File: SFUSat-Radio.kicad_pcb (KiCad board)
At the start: 4 copper layers, 95.9 x 90.2 mm, 279 parts, among them J1 PC104-8BIT, J10 TP_TH_150, J11 TP_TH_150, J12 SMA, J13 SMA, J14 SMA, J15 Conn_01x02, J16 SMA, J17 SMA, J18 SMA, J19 Conn_01x03, J2 PC104PTH, J20 Conn_01x03, J21 TP_TH_150, J22 TP_TH_150, J23 TP_TH_150, J24 TP_TH_150, J25 Conn_01x02, J3 PC104PTH, J4 PC104PTH, J400 SMA, J401 TP_TH_150, J402 TP_TH_150, J404 TP_TH_150, J405 TP_TH_150, J406 TP_TH_150, J5 PC104PTH, J500 SMA, J501 TP_TH_150, J502 TP_TH_150, J504 TP_TH_150, J505 TP_TH_150, J506 TP_TH_150, J6 SMA, J7 TP_TH_150, J8 TP_TH_150, J9 TP_TH_150, U1 SINGLE_0402, U10 TPS799, U100 CC1101-Q1, U101 0433BM15A0001, U11 SINGLE_0402, U110 CC1101-Q1, U111 0915BM15A0001E, U12 CONN_02X05_SHRD, U13 CONN_02X05_SHRD, U14 2N7002DW, U15 TPS62175DQCR, U16 TPS71750DSER, U17 74LVC1G14SE-7, U2 SKY13345-368LF, U3 CD4555BPWR, U4 LMS3635AQRNLRQ1, U400 SINGLE_0402, U401 LMV358, U402 RF6886, U420 2N7002DW, U5 MML09211H, U500 SINGLE_0402, U501 LMV358, U502 RF6886, U6 SINGLE_0402, U600 STLM75, U610 STLM75, U7 SKY13372-467LF, U8 SINGLE_0402, U9 TLV702, X100 NX3225GA, X110 NX3225GA

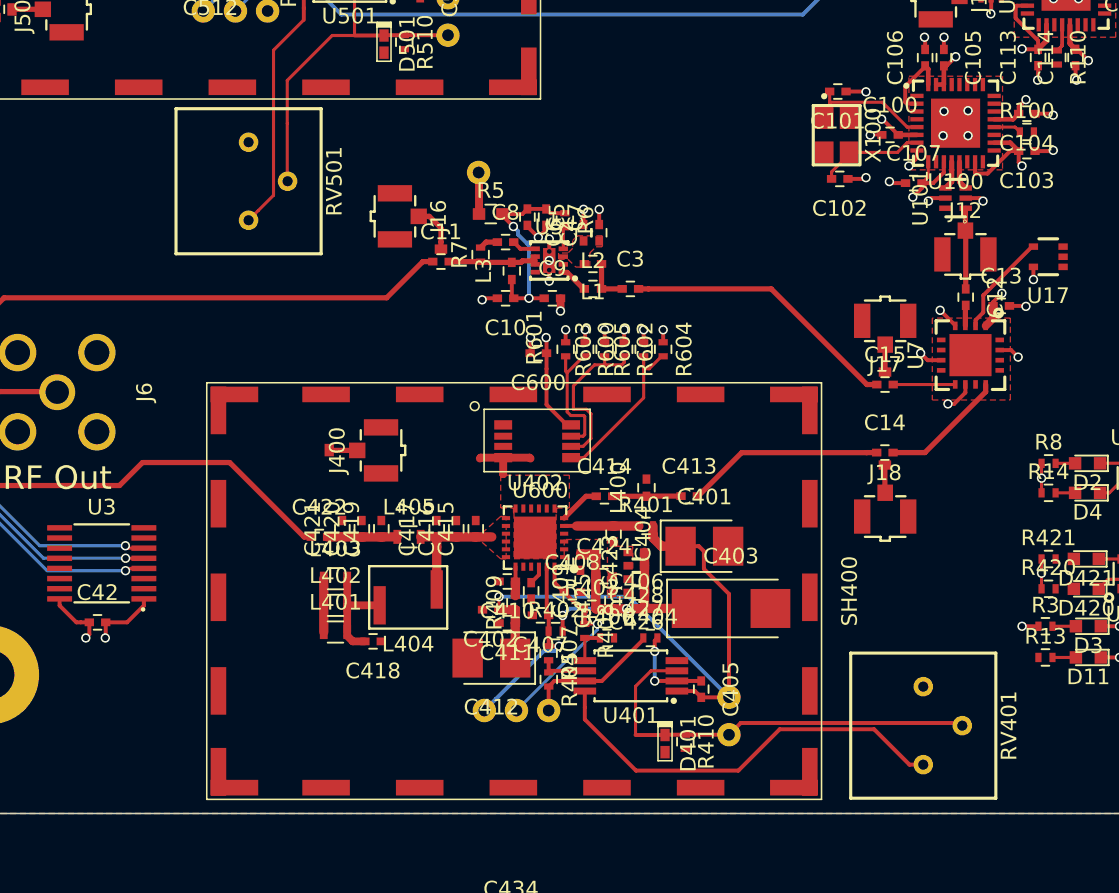
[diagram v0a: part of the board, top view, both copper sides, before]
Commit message: added optional gain select resistor
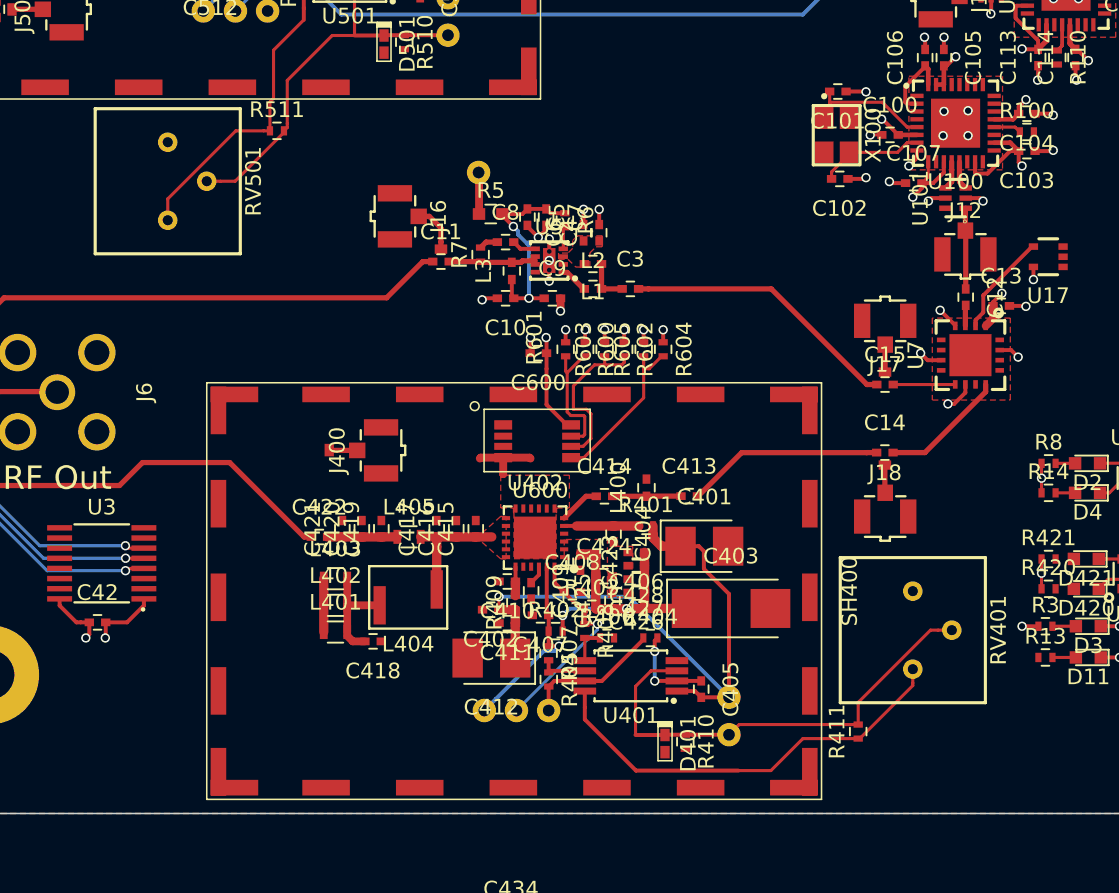
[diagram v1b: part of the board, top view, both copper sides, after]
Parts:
- added R411: DNP, SFUSat:R_0402, F.Cu at (173.2, 143.2)
- added R511: DNP, SFUSat:R_0402, F.Cu at (136.0, 104.8)
- moved RV401 6.16 mm to (176.8, 136.8)
- moved RV501 5.18 mm to (129.0, 108.0)
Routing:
- net /3V1: track 111.6 -> 115.7 mm
- net /PA_UB/GAIN: track 24.2 -> 27.4 mm
- net /PA_LB/GAIN: track 27.5 -> 30.1 mm
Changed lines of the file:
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@@
 (kicad_pcb (version 4) (host pcbnew 4.0.7-e2-6376~58~ubuntu16.04.1)
   (general
-    (links 720)
-    (no_connects 107)
-    (area 45.1 55.986 358.142847 234.47)
+    (links 724)
+    (no_connects 99)
+    (area 112.449999 58.279999 208.440001 148.550001)
     (thickness 1.6)
     (drawings 18)
-    (tracks 1119)
+    (tracks 1132)
     (zones 0)
-    (modules 279)
+    (modules 281)
     (nets 207)
   )
@@
   )
   (setup
-    (last_trace_width 0.254)
+    (last_trace_width 0.2)
     (user_trace_width 0.1524)
     (user_trace_width 0.2)
@@
   )
   (module SFUSat:CT6EP103 locked (layer F.Cu)
-    (at 177.42 142.87 270)
+    (at 176.75 136.75 270)
     (fp_text reference RV401 (at 0 -5.5 270) (layer F.SilkS)
       (effects (font (size 1 1) (thickness 0.15)))
@@
   )
   (module SFUSat:CT6EP103 locked (layer F.Cu)
-    (at 134.18 107.98 270)
+    (at 129 107.98 270)
     (fp_text reference RV501 (at 0 -5.5 270) (layer F.SilkS)
       (effects (font (size 1 1) (thickness 0.15)))
@@
     )
   )
+  (module SFUSat:R_0402 (layer F.Cu)
+    (at 173.25 143.25 90)
+    (descr "Resistor SMD 0402, reflow soldering, Vishay (see dcrcw.pdf)")
+    (tags "resistor 0402")
+    (attr smd)
+    (fp_text reference R411 (at 0 -1.35 90) (layer F.SilkS)
+      (effects (font (size 1 1) (thickness 0.15)))
+    )
+    (fp_text value DNP (at 0 1.45 90) (layer F.Fab)
+      (effects (font (size 1 1) (thickness 0.15)))
+    )
+    (fp_text user %R (at 0 -1.35 90) (layer F.Fab)
+      (effects (font (size 1 1) (thickness 0.15)))
+    )
+    (fp_line (start -0.5 0.25) (end -0.5 -0.25) (layer F.Fab) (width 0.1))
+    (fp_line (start 0.5 0.25) (end -0.5 0.25) (layer F.Fab) (width 0.1))
+    (fp_line (start 0.5 -0.25) (end 0.5 0.25) (layer F.Fab) (width 0.1))
+    (fp_line (start -0.5 -0.25) (end 0.5 -0.25) (layer F.Fab) (width 0.1))
+    (fp_line (start 0.25 -0.53) (end -0.25 -0.53) (layer F.SilkS) (width 0.12))
+    (fp_line (start -0.25 0.53) (end 0.25 0.53) (layer F.SilkS) (width 0.12))
+    (fp_line (start -0.8 -0.45) (end 0.8 -0.45) (layer F.CrtYd) (width 0.05))
+    (fp_line (start -0.8 -0.45) (end -0.8 0.45) (layer F.CrtYd) (width 0.05))
+    (fp_line (start 0.8 0.45) (end 0.8 -0.45) (layer F.CrtYd) (width 0.05))
+    (fp_line (start 0.8 0.45) (end -0.8 0.45) (layer F.CrtYd) (width 0.05))
+    (pad 1 smd rect (at -0.45 0 90) (size 0.4 0.6) (layers F.Cu F.Paste F.Mask)
+      (net 116 /3V1) (solder_paste_margin -0.02))
+    (pad 2 smd rect (at 0.45 0 90) (size 0.4 0.6) (layers F.Cu F.Paste F.Mask)
+      (net 103 /PA_LB/GAIN) (solder_paste_margin -0.02))
+    (model Resistors_SMD.3dshapes/R_0402.wrl
+      (at (xyz 0 0 0))
+      (scale (xyz 1 1 1))
+      (rotate (xyz 0 0 0))
+    )
+  )
+  (module SFUSat:R_0402 (layer F.Cu)
+    (at 136 104.75)
+    (descr "Resistor SMD 0402, reflow soldering, Vishay (see dcrcw.pdf)")
+    (tags "resistor 0402")
+    (attr smd)
+    (fp_text reference R511 (at 0 -1.35) (layer F.SilkS)
+      (effects (font (size 1 1) (thickness 0.15)))
+    )
+    (fp_text value DNP (at 0 1.45) (layer F.Fab)
+      (effects (font (size 1 1) (thickness 0.15)))
+    )
+    (fp_text user %R (at 0 -1.35) (layer F.Fab)
+      (effects (font (size 1 1) (thickness 0.15)))
+    )
+    (fp_line (start -0.5 0.25) (end -0.5 -0.25) (layer F.Fab) (width 0.1))
+    (fp_line (start 0.5 0.25) (end -0.5 0.25) (layer F.Fab) (width 0.1))
+    (fp_line (start 0.5 -0.25) (end 0.5 0.25) (layer F.Fab) (width 0.1))
+    (fp_line (start -0.5 -0.25) (end 0.5 -0.25) (layer F.Fab) (width 0.1))
+    (fp_line (start 0.25 -0.53) (end -0.25 -0.53) (layer F.SilkS) (width 0.12))
+    (fp_line (start -0.25 0.53) (end 0.25 0.53) (layer F.SilkS) (width 0.12))
+    (fp_line (start -0.8 -0.45) (end 0.8 -0.45) (layer F.CrtYd) (width 0.05))
+    (fp_line (start -0.8 -0.45) (end -0.8 0.45) (layer F.CrtYd) (width 0.05))
+    (fp_line (start 0.8 0.45) (end 0.8 -0.45) (layer F.CrtYd) (width 0.05))
+    (fp_line (start 0.8 0.45) (end -0.8 0.45) (layer F.CrtYd) (width 0.05))
+    (pad 1 smd rect (at -0.45 0) (size 0.4 0.6) (layers F.Cu F.Paste F.Mask)
+      (net 116 /3V1) (solder_paste_margin -0.02))
+    (pad 2 smd rect (at 0.45 0) (size 0.4 0.6) (layers F.Cu F.Paste F.Mask)
+      (net 108 /PA_UB/GAIN) (solder_paste_margin -0.02))
+    (model Resistors_SMD.3dshapes/R_0402.wrl
+      (at (xyz 0 0 0))
+      (scale (xyz 1 1 1))
+      (rotate (xyz 0 0 0))
+    )
+  )
   (dimension 9.4 (width 0.3) (layer Dwgs.User)
     (gr_text "9.400 mm" (at 117.2 117.85) (layer Dwgs.User)
@@
   (segment (start 191.529999 127.349999) (end 191.63 127.45) (width 0.2) (layer F.Cu) (net 102))
   (segment (start 191.63 127.45) (end 191.63 127.95) (width 0.2) (layer F.Cu) (net 102))
-  (segment (start 164.97 143.45) (end 165.719999 142.700001) (width 0.254) (layer F.Cu) (net 103))
-  (segment (start 165.719999 142.700001) (end 179.750001 142.700001) (width 0.254) (layer F.Cu) (net 103))
-  (segment (start 179.750001 142.700001) (end 179.92 142.87) (width 0.2) (layer F.Cu) (net 103))
+  (segment (start 173.25 142.8) (end 173.25 141.380998) (width 0.2) (layer F.Cu) (net 103))
+  (segment (start 173.25 141.380998) (end 177.880998 136.75) (width 0.2) (layer F.Cu) (net 103))
+  (segment (start 178.366117 136.75) (end 179.25 136.75) (width 0.2) (layer F.Cu) (net 103))
+  (segment (start 177.880998 136.75) (end 178.366117 136.75) (width 0.2) (layer F.Cu) (net 103))
+  (segment (start 173.25 142.8) (end 165.62 142.8) (width 0.2) (layer F.Cu) (net 103))
+  (segment (start 165.62 142.8) (end 164.97 143.45) (width 0.2) (layer F.Cu) (net 103))
   (segment (start 162.17 143.45) (end 162.67 143.45) (width 0.254) (layer F.Cu) (net 103))
   (segment (start 162.67 143.45) (end 164.97 143.45) (width 0.254) (layer F.Cu) (net 103))
@@
   (segment (start 190.07 132.19) (end 188.676429 132.19) (width 0.2) (layer F.Cu) (net 107))
   (segment (start 188.676429 132.19) (end 188.671429 132.185) (width 0.2) (layer F.Cu) (net 107))
-  (segment (start 136.66 104.27) (end 136.66 107.96) (width 0.2) (layer F.Cu) (net 108))
-  (segment (start 136.66 107.96) (end 136.68 107.98) (width 0.1524) (layer F.Cu) (net 108))
+  (segment (start 136.45 104.75) (end 136.45 104.85) (width 0.2) (layer F.Cu) (net 108))
+  (segment (start 136.45 104.85) (end 133.32 107.98) (width 0.2) (layer F.Cu) (net 108))
+  (segment (start 133.32 107.98) (end 132.383883 107.98) (width 0.2) (layer F.Cu) (net 108))
+  (segment (start 132.383883 107.98) (end 131.5 107.98) (width 0.2) (layer F.Cu) (net 108))
+  (segment (start 136.66 104.27) (end 136.66 104.54) (width 0.2) (layer F.Cu) (net 108))
+  (segment (start 136.66 104.54) (end 136.45 104.75) (width 0.2) (layer F.Cu) (net 108))
   (segment (start 136.66 104.27) (end 136.68 104.29) (width 0.1524) (layer F.Cu) (net 108))
   (segment (start 136.66 101.52) (end 136.66 104.27) (width 0.2) (layer F.Cu) (net 108))
@@
   (segment (start 118.31 121.46) (end 117.45 121.46) (width 0.336) (layer F.Cu) (net 115))
   (segment (start 118.31 121.46) (end 121.87 121.46) (width 0.336) (layer F.Cu) (net 115))
+  (segment (start 173.25 143.7) (end 173.35 143.7) (width 0.2) (layer F.Cu) (net 116))
+  (segment (start 173.35 143.7) (end 176.75 140.3) (width 0.2) (layer F.Cu) (net 116))
+  (segment (start 176.75 140.3) (end 176.75 140.133883) (width 0.2) (layer F.Cu) (net 116))
+  (segment (start 176.75 140.133883) (end 176.75 139.25) (width 0.2) (layer F.Cu) (net 116))
+  (segment (start 173.25 143.7) (end 169.704998 143.7) (width 0.2) (layer F.Cu) (net 116))
+  (segment (start 169.704998 143.7) (end 167.654998 145.75) (width 0.2) (layer F.Cu) (net 116))
+  (segment (start 167.654998 145.75) (end 165.57 145.75) (width 0.2) (layer F.Cu) (net 116))
+  (segment (start 129 110.48) (end 129 109.110998) (width 0.2) (layer F.Cu) (net 116))
+  (segment (start 129 109.110998) (end 133.360998 104.75) (width 0.2) (layer F.Cu) (net 116))
+  (segment (start 133.360998 104.75) (end 135.15 104.75) (width 0.2) (layer F.Cu) (net 116))
+  (segment (start 135.15 104.75) (end 135.55 104.75) (width 0.2) (layer F.Cu) (net 116))
+  (segment (start 135.78 102.67) (end 135.55 102.9) (width 0.2) (layer F.Cu) (net 116))
+  (segment (start 135.55 102.9) (end 135.55 104.75) (width 0.2) (layer F.Cu) (net 116))
   (segment (start 192.25 78.75) (end 192.25 81.75) (width 0.254) (layer B.Cu) (net 116))
   (segment (start 192.25 81.75) (end 187.75 86.25) (width 0.254) (layer B.Cu) (net 116))
@@
   (segment (start 190.324898 80.108344) (end 190.299898 80.083344) (width 0.2) (layer F.Cu) (net 116))
   (segment (start 135.78 102.67) (end 135.778799 102.671201) (width 0.1524) (layer F.Cu) (net 116))
-  (segment (start 135.778799 102.671201) (end 135.778799 108.881201) (width 0.2) (layer F.Cu) (net 116))
-  (segment (start 135.778799 108.881201) (end 134.804999 109.855001) (width 0.2) (layer F.Cu) (net 116))
-  (segment (start 134.804999 109.855001) (end 134.18 110.48) (width 0.2) (layer F.Cu) (net 116))
   (segment (start 165.57 145.75) (end 159.01 145.75) (width 0.254) (layer F.Cu) (net 116))
   (segment (start 159.01 145.75) (end 155.73 142.47) (width 0.254) (layer F.Cu) (net 116))
-  (segment (start 168.219989 143.100011) (end 165.57 145.75) (width 0.254) (layer F.Cu) (net 116))
-  (segment (start 174.266128 143.100011) (end 168.219989 143.100011) (width 0.254) (layer F.Cu) (net 116))
-  (segment (start 177.42 145.37) (end 176.536117 145.37) (width 0.254) (layer F.Cu) (net 116))
-  (segment (start 176.536117 145.37) (end 174.266128 143.100011) (width 0.254) (layer F.Cu) (net 116))
   (segment (start 135.78 102.67) (end 135.78 99.58) (width 0.2) (layer F.Cu) (net 116))
   (segment (start 135.78 99.58) (end 137.72 97.64) (width 0.2) (layer F.Cu) (net 116))

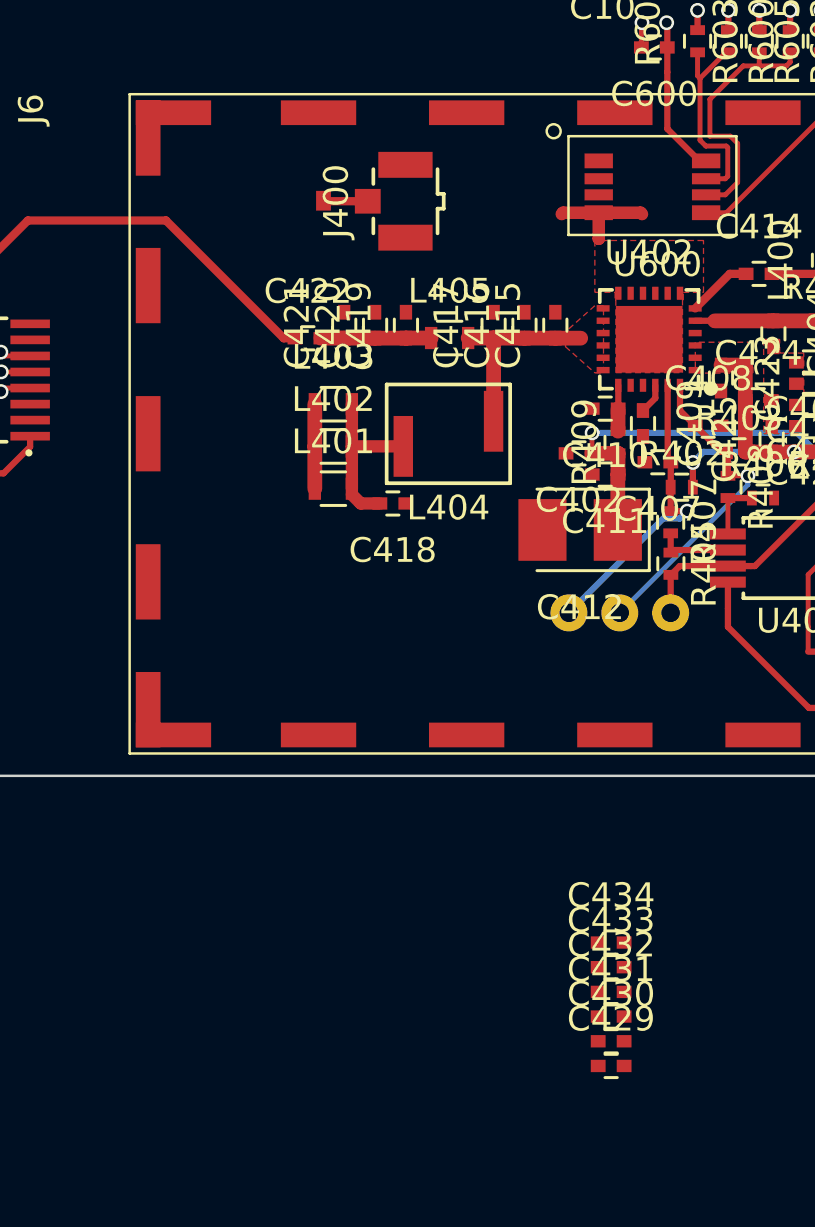
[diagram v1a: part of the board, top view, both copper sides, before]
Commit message: placed optional PA filtering to LB
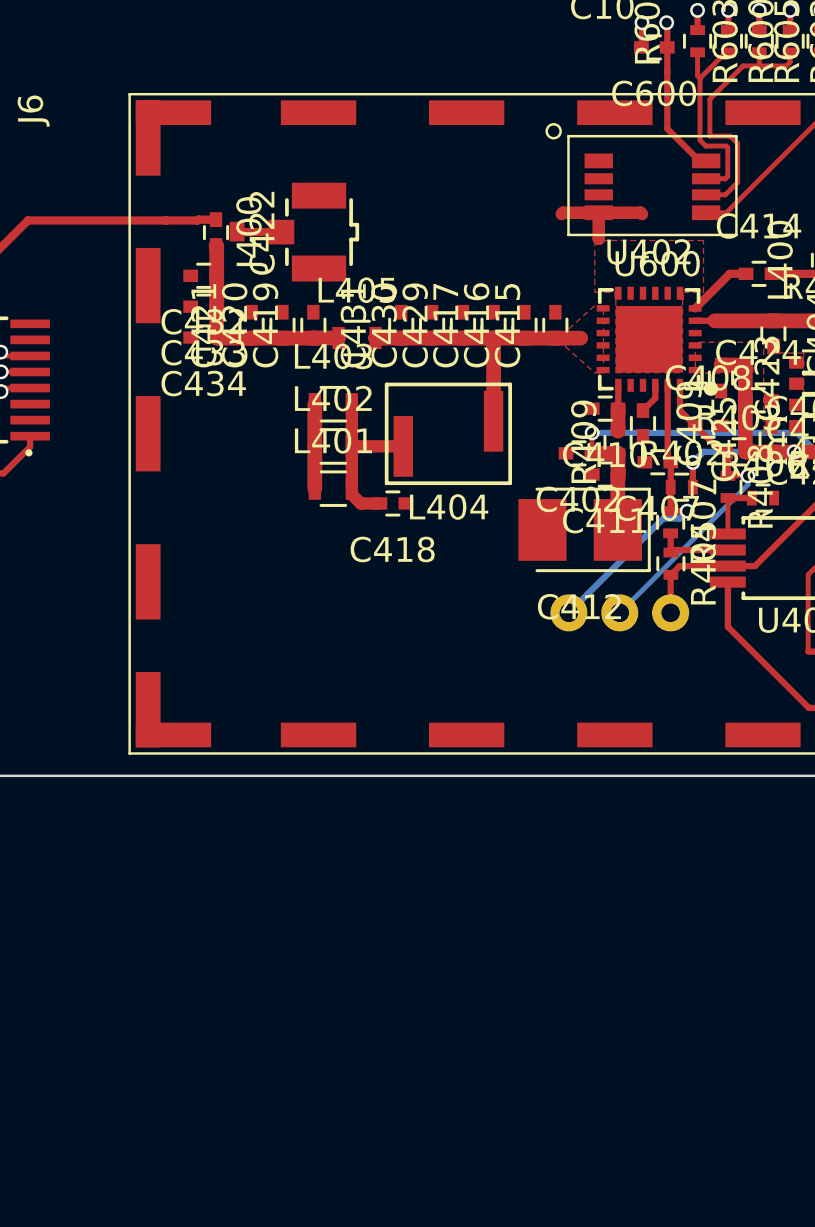
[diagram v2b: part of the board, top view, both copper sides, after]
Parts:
- moved C432 33.4 mm to (134.5, 128.2), turned to 180 degrees
- moved C433 31.4 mm to (134.5, 129.5), turned to 180 degrees
- moved C429 30.6 mm to (145.0, 130.2), turned to 90 degrees
- moved C430 29.9 mm to (143.8, 130.2), turned to 90 degrees
- moved C434 29.5 mm to (134.5, 130.8), turned to 180 degrees
- moved C431 29.3 mm to (142.5, 130.2), turned to 90 degrees
- moved C422 5.67 mm to (135.0, 126.5), turned to 270 degrees
- moved C419 3.75 mm to (138.9, 130.2)
- moved C420 3.75 mm to (137.7, 130.2)
- moved C421 3.75 mm to (136.4, 130.2)
- moved L405 3.75 mm to (140.7, 130.8)
- moved J400 3.72 mm to (139.2, 126.5)
- moved U400 3.72 mm to (135.8, 126.5)
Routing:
- net /LB_HP_TX: track 28.8 -> 23.6 mm
- net /LB_TEST_TX: track 4.47 -> 8.68 mm
- net /PA_LB/OUT: track 7.93 -> 11.7 mm

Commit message: layed out indicator lights
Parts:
- added D1: GREEN, SFUSat:LED_0603, F.Cu at (175.2, 142.8)
- added R18: 287, SFUSat:R_0402, F.Cu at (173.8, 143.0)
- moved J11 117.9 mm to (152.8, 61.8)
- moved J9 69.2 mm to (174.8, 145.8), turned to 90 degrees
- moved J7 60.0 mm to (177.2, 145.8), turned to 90 degrees
- moved J21 56.5 mm to (182.2, 145.8), turned to 270 degrees
- moved J24 54.1 mm to (189.8, 145.8), turned to 270 degrees
- moved J22 52.0 mm to (187.8, 145.8), turned to 270 degrees
- moved J8 22.1 mm to (180.2, 145.8), turned to 270 degrees
- moved U14 19.0 mm to (192.5, 146.0), turned to 90 degrees
- moved R8 18.1 mm to (191.8, 143.0), turned to 90 degrees
- moved D2 17.7 mm to (193.2, 142.9), turned to 90 degrees
- moved J23 16.3 mm to (195.2, 145.8), turned to 270 degrees
- moved R14 15.4 mm to (188.8, 143.0), turned to 90 degrees
- moved D4 15.2 mm to (190.2, 142.9), turned to 90 degrees
- moved R411 14.9 mm to (184.0, 133.0)
- moved U420 13.8 mm to (185.0, 145.7), turned to 270 degrees
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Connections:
- J24 pad 1: /Indicator2/G2 -> /5V0
- U14 pad 2: /Indicator2/G2 -> /5V0
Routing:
- net /3V1: track 115.7 -> 96.1 mm, vias 1 -> 2
- net /PA_LB/GAIN: track 30.1 -> 12.2 mm
- net GND: track 109.5 -> 119.7 mm, vias 89 -> 95
- net /5V0: track 5.12 -> 12.1 mm, vias 0 -> 1
- net /LB_RX0TX1: track 0.00 -> 6.58 mm, vias 0 -> 1
- net /PKT_RCV: track 0.00 -> 6.48 mm
- net /UB_RX0TX1: track 2.11 -> 6.23 mm
- net /3V6: track 65.9 -> 68.4 mm
- net Net-(D1-Pad2): track 0.00 -> 1.75 mm
- net Net-(D420-Pad2): track 0.00 -> 1.70 mm
- net Net-(D421-Pad2): track 0.00 -> 1.61 mm
- net Net-(D421-Pad1): track 1.40 -> 2.32 mm
- net /3V3: track 37.1 -> 38.0 mm, vias 15 -> 16
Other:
- board text added: "3.1V"
- board text added: "3.3V"
- board text added: "3.6V"
- board text added: "5.0V"
- board text added: "GND"
- board text added: "LB_TX"
- board text added: "RX"
- board text added: "UB_TX"
